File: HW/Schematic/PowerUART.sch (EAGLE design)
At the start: 62 parts, among them U2 CP2104

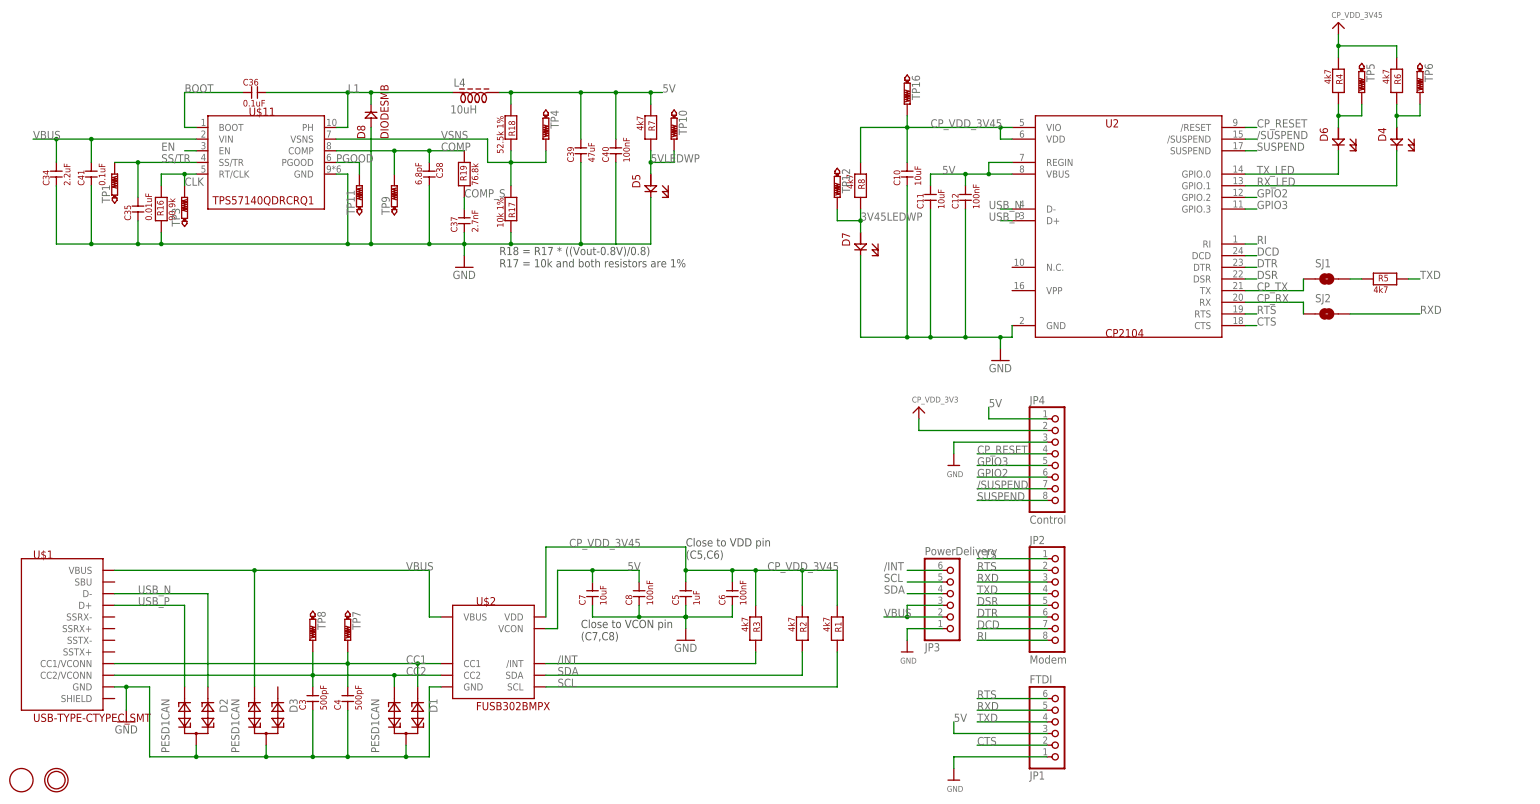
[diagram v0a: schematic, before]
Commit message: Add labels
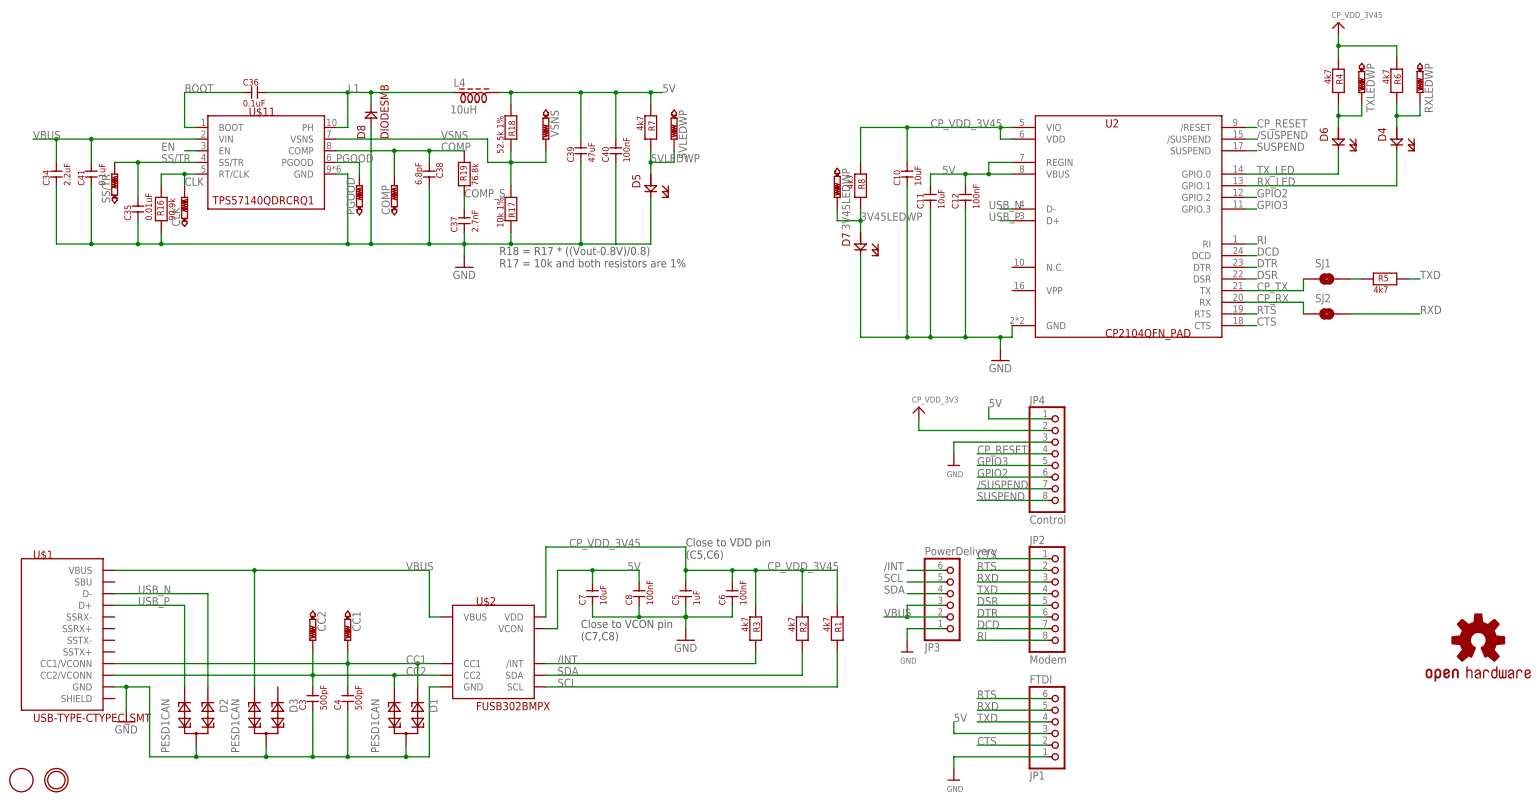
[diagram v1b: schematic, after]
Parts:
- removed TP16: CP_RESET, testpad:PTR1B1,27
- added LOGO1: OSHW-LOGOMINI, IO_expander:OSHW-LOGOMINI
- U2: value CP2104 -> CP2104QFN_PAD; device CP2104:CP2104 -> CP2104:CP2104QFN_PAD
- renumbered TP1 to SS/TR, TP10 to 5VLEDWP, TP11 to PGOOD, TP12 to 3V45LEDWP, TP3 to CLK, TP4 to VSNS, TP5 to TXLEDWP, TP6 to RXLEDWP, TP7 to CC1, TP8 to CC2, TP9 to COMP
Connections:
- net CP_VDD_3V45: no longer TP16.TP
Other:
- moved on the sheet: U2

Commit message: add testpoints.csv
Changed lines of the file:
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@@
 <grid distance="0.1" unitdist="inch" unit="inch" style="lines" multiple="1" display="no" altdistance="0.01" altunitdist="inch" altunit="inch"/>
 <layers>
-<layer number="1" name="Top" color="4" fill="1" visible="yes" active="no"/>
-<layer number="2" name="Route2" color="1" fill="3" visible="yes" active="no"/>
-<layer number="3" name="Route3" color="4" fill="3" visible="yes" active="no"/>
-<layer number="4" name="Route4" color="1" fill="4" visible="yes" active="no"/>
-<layer number="5" name="Route5" color="4" fill="4" visible="yes" active="no"/>
-<layer number="6" name="Route6" color="1" fill="8" visible="yes" active="no"/>
-<layer number="7" name="Route7" color="4" fill="8" visible="yes" active="no"/>
-<layer number="8" name="Route8" color="1" fill="2" visible="yes" active="no"/>
-<layer number="9" name="Route9" color="4" fill="2" visible="yes" active="no"/>
-<layer number="10" name="Route10" color="1" fill="7" visible="yes" active="no"/>
-<layer number="11" name="Route11" color="4" fill="7" visible="yes" active="no"/>
-<layer number="12" name="Route12" color="1" fill="5" visible="yes" active="no"/>
-<layer number="13" name="Route13" color="4" fill="5" visible="yes" active="no"/>
-<layer number="14" name="Route14" color="1" fill="6" visible="yes" active="no"/>
-<layer number="15" name="Route15" color="4" fill="6" visible="yes" active="no"/>
-<layer number="16" name="Bottom" color="1" fill="1" visible="yes" active="no"/>
-<layer number="17" name="Pads" color="2" fill="1" visible="yes" active="no"/>
-<layer number="18" name="Vias" color="2" fill="1" visible="yes" active="no"/>
-<layer number="19" name="Unrouted" color="6" fill="1" visible="yes" active="no"/>
-<layer number="20" name="Dimension" color="24" fill="1" visible="yes" active="no"/>
-<layer number="21" name="tPlace" color="7" fill="1" visible="yes" active="no"/>
-<layer number="22" name="bPlace" color="7" fill="1" visible="yes" active="no"/>
-<layer number="23" name="tOrigins" color="15" fill="1" visible="yes" active="no"/>
-<layer number="24" name="bOrigins" color="15" fill="1" visible="yes" active="no"/>
-<layer number="25" name="tNames" color="7" fill="1" visible="yes" active="no"/>
-<layer number="26" name="bNames" color="7" fill="1" visible="yes" active="no"/>
-<layer number="27" name="tValues" color="7" fill="1" visible="yes" active="no"/>
-<layer number="28" name="bValues" color="7" fill="1" visible="yes" active="no"/>
+<layer number="1" name="Top" color="4" fill="1" visible="no" active="no"/>
+<layer number="2" name="Route2" color="1" fill="3" visible="no" active="no"/>
+<layer number="3" name="Route3" color="4" fill="3" visible="no" active="no"/>
+<layer number="4" name="Route4" color="1" fill="4" visible="no" active="no"/>
+<layer number="5" name="Route5" color="4" fill="4" visible="no" active="no"/>
+<layer number="6" name="Route6" color="1" fill="8" visible="no" active="no"/>
+<layer number="7" name="Route7" color="4" fill="8" visible="no" active="no"/>
+<layer number="8" name="Route8" color="1" fill="2" visible="no" active="no"/>
+<layer number="9" name="Route9" color="4" fill="2" visible="no" active="no"/>
+<layer number="10" name="Route10" color="1" fill="7" visible="no" active="no"/>
+<layer number="11" name="Route11" color="4" fill="7" visible="no" active="no"/>
+<layer number="12" name="Route12" color="1" fill="5" visible="no" active="no"/>
+<layer number="13" name="Route13" color="4" fill="5" visible="no" active="no"/>
+<layer number="14" name="Route14" color="1" fill="6" visible="no" active="no"/>
+<layer number="15" name="Route15" color="4" fill="6" visible="no" active="no"/>
+<layer number="16" name="Bottom" color="1" fill="1" visible="no" active="no"/>
+<layer number="17" name="Pads" color="2" fill="1" visible="no" active="no"/>
+<layer number="18" name="Vias" color="2" fill="1" visible="no" active="no"/>
+<layer number="19" name="Unrouted" color="6" fill="1" visible="no" active="no"/>
+<layer number="20" name="Dimension" color="24" fill="1" visible="no" active="no"/>
+<layer number="21" name="tPlace" color="7" fill="1" visible="no" active="no"/>
+<layer number="22" name="bPlace" color="7" fill="1" visible="no" active="no"/>
+<layer number="23" name="tOrigins" color="15" fill="1" visible="no" active="no"/>
+<layer number="24" name="bOrigins" color="15" fill="1" visible="no" active="no"/>
+<layer number="25" name="tNames" color="7" fill="1" visible="no" active="no"/>
+<layer number="26" name="bNames" color="7" fill="1" visible="no" active="no"/>
+<layer number="27" name="tValues" color="7" fill="1" visible="no" active="no"/>
+<layer number="28" name="bValues" color="7" fill="1" visible="no" active="no"/>
 <layer number="29" name="tStop" color="7" fill="3" visible="no" active="no"/>
 <layer number="30" name="bStop" color="7" fill="6" visible="no" active="no"/>
@@
 <layer number="35" name="tGlue" color="7" fill="4" visible="no" active="no"/>
 <layer number="36" name="bGlue" color="7" fill="5" visible="no" active="no"/>
-<layer number="37" name="tTest" color="7" fill="1" visible="yes" active="no"/>
-<layer number="38" name="bTest" color="7" fill="1" visible="yes" active="no"/>
+<layer number="37" name="tTest" color="7" fill="1" visible="no" active="no"/>
+<layer number="38" name="bTest" color="7" fill="1" visible="no" active="no"/>
 <layer number="39" name="tKeepout" color="4" fill="11" visible="no" active="no"/>
 <layer number="40" name="bKeepout" color="1" fill="11" visible="no" active="no"/>
@@
 <layer number="44" name="Drills" color="7" fill="1" visible="no" active="no"/>
 <layer number="45" name="Holes" color="7" fill="1" visible="no" active="no"/>
-<layer number="46" name="Milling" color="3" fill="1" visible="yes" active="no"/>
-<layer number="47" name="Measures" color="7" fill="1" visible="yes" active="no"/>
-<layer number="48" name="Document" color="7" fill="1" visible="yes" active="no"/>
-<layer number="49" name="Reference" color="7" fill="1" visible="yes" active="no"/>
-<layer number="50" name="dxf" color="7" fill="1" visible="yes" active="no"/>
-<layer number="51" name="tDocu" color="7" fill="1" visible="yes" active="no"/>
-<layer number="52" name="bDocu" color="7" fill="1" visible="yes" active="no"/>
-<layer number="53" name="tGND_GNDA" color="7" fill="9" visible="yes" active="no"/>
-<layer number="54" name="bGND_GNDA" color="1" fill="9" visible="yes" active="no"/>
-<layer number="56" name="wert" color="7" fill="1" visible="yes" active="no"/>
-<layer number="57" name="tCAD" color="7" fill="1" visible="yes" active="no"/>
-<layer number="58" name="bCAD" color="7" fill="1" visible="yes" active="no"/>
-<layer number="59" name="tCarbon" color="7" fill="1" visible="yes" active="no"/>
-<layer number="60" name="bCarbon" color="7" fill="1" visible="yes" active="no"/>
+<layer number="46" name="Milling" color="3" fill="1" visible="no" active="no"/>
+<layer number="47" name="Measures" color="7" fill="1" visible="no" active="no"/>
+<layer number="48" name="Document" color="7" fill="1" visible="no" active="no"/>
+<layer number="49" name="Reference" color="7" fill="1" visible="no" active="no"/>
+<layer number="50" name="dxf" color="7" fill="1" visible="no" active="no"/>
+<layer number="51" name="tDocu" color="7" fill="1" visible="no" active="no"/>
+<layer number="52" name="bDocu" color="7" fill="1" visible="no" active="no"/>
+<layer number="53" name="tGND_GNDA" color="7" fill="9" visible="no" active="no"/>
+<layer number="54" name="bGND_GNDA" color="1" fill="9" visible="no" active="no"/>
+<layer number="56" name="wert" color="7" fill="1" visible="no" active="no"/>
+<layer number="57" name="tCAD" color="7" fill="1" visible="no" active="no"/>
+<layer number="58" name="bCAD" color="7" fill="1" visible="no" active="no"/>
+<layer number="59" name="tCarbon" color="7" fill="1" visible="no" active="no"/>
+<layer number="60" name="bCarbon" color="7" fill="1" visible="no" active="no"/>
 <layer number="88" name="SimResults" color="9" fill="1" visible="yes" active="yes"/>
 <layer number="89" name="SimProbes" color="9" fill="1" visible="yes" active="yes"/>
@@
 <part name="JP1" library="microbuilder" deviceset="HEADER-1X6" device="76MIL" value="FTDI"/>
 <part name="U$12" library="microbuilder" deviceset="GND" device=""/>
-<part name="U$15" library="microbuilder" deviceset="3.3V" device="" value="CP_VDD_3V3"/>
+<part name="U$15" library="microbuilder" deviceset="3.3V" device="" value="CP_VDD_3V45"/>
 <part name="U$16" library="microbuilder" deviceset="GND" device=""/>
 <part name="JP4" library="microbuilder" deviceset="HEADER-1X8" device="70MIL" value="Control"/>
